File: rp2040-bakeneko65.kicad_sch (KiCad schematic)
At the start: 27 parts, among them J1 SM04B-SRSS-TB, SW1 SW_Push, U1 RP2040, U2 W25Q128JVS, U3 XC6206PxxxMR, Y1 12MHz

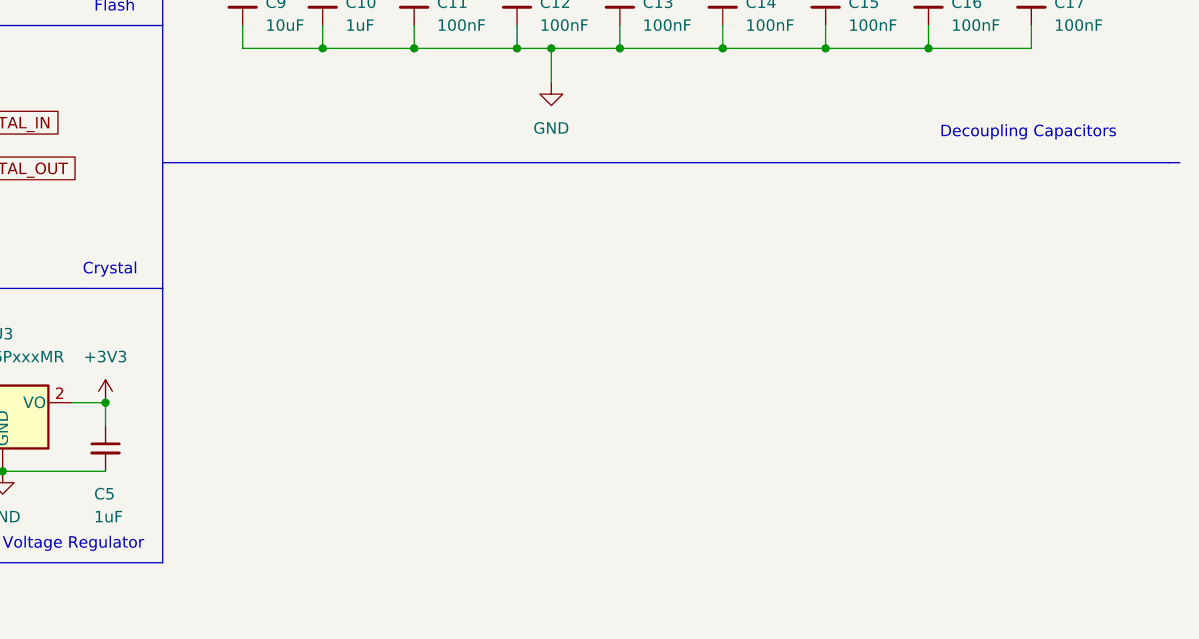
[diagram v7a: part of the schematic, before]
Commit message: Add subsheet
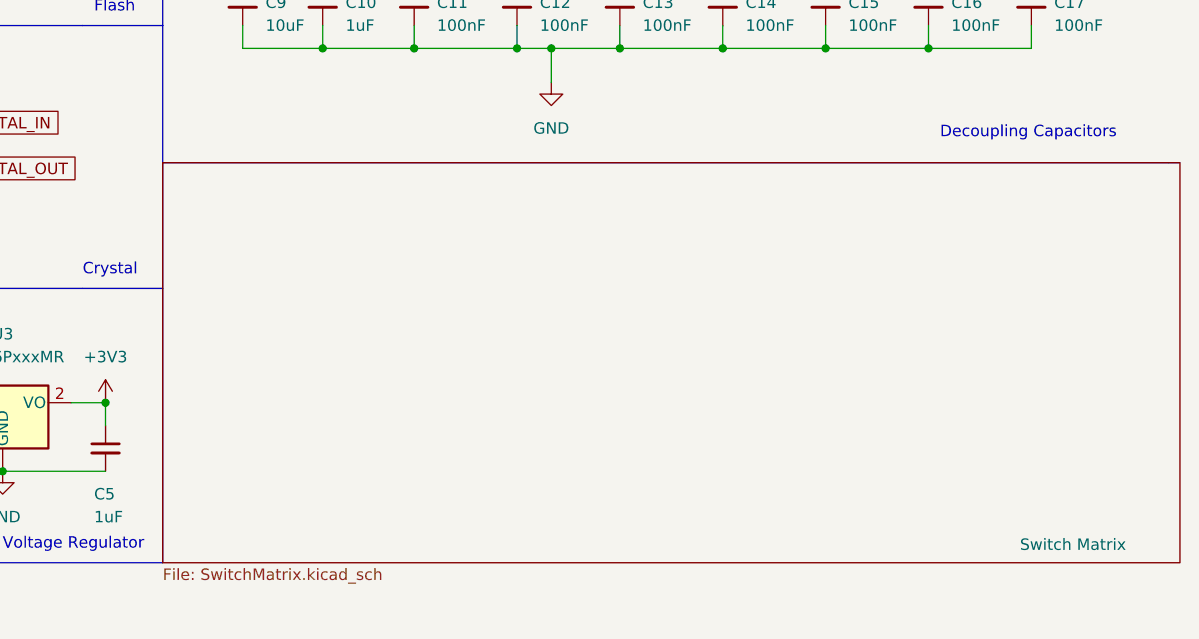
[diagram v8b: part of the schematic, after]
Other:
- added sheet Switch Matrix (SwitchMatrix.kicad_sch)
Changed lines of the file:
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@@
     (pin "2")
+  )
+  (sheet (at 173.99 68.58) (size 113.03 44.45)
+    (stroke (width 0.1524) (type solid) (color 0 0 0 0))
+    (fill (color 0 0 0 0.0000))
+    (property "Sheet name" "Switch Matrix" (id 0) (at 269.24 111.76 0)
+      (effects (font (size 1.27 1.27)) (justify left bottom))
+    )
+    (property "Sheet file" "SwitchMatrix.kicad_sch" (id 1) (at 173.99 113.6146 0)
+      (effects (font (size 1.27 1.27)) (justify left top))
+    )
   )
   (sheet_instances
     (path "/" (page "1"))
+    (path "/fb7c2ffa-ca99-4b61-b7b2-daf423069bae" (page "2"))
   )
   (symbol_instances
